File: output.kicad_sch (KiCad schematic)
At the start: 15 parts, among them P12 Conn_01x03_Socket, P13 Conn_01x03_Socket, P14 Conn_01x03_Socket, P27 Conn_01x03_Socket, U4 ULN2003AID

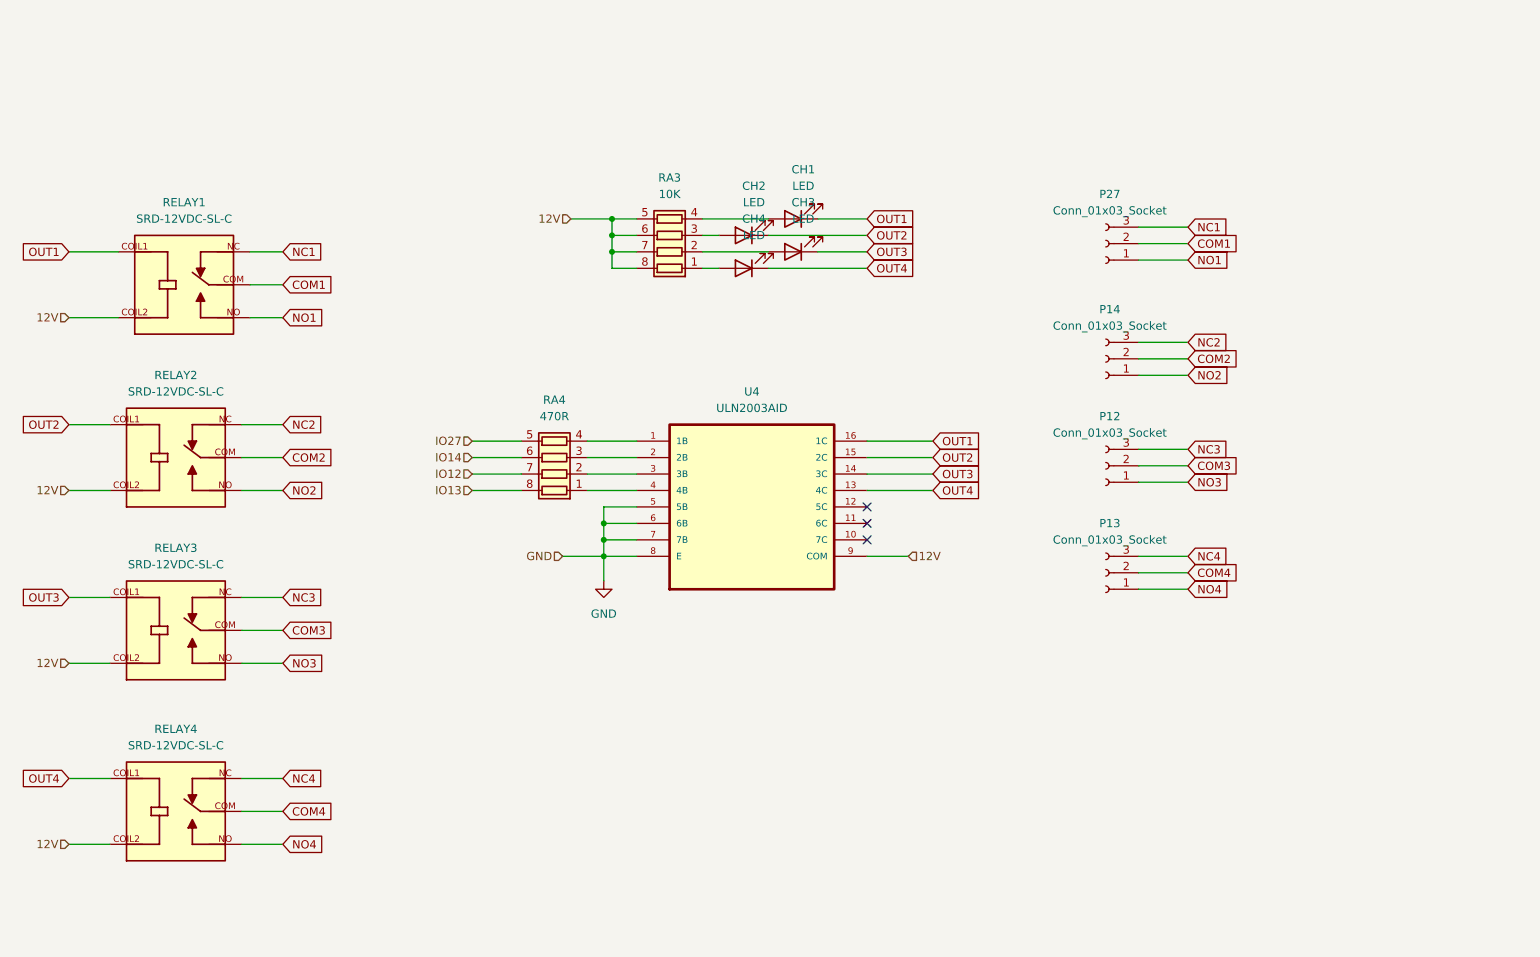
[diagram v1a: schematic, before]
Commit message: relacion de gpios, inicio de esquematico-salidas en proceso
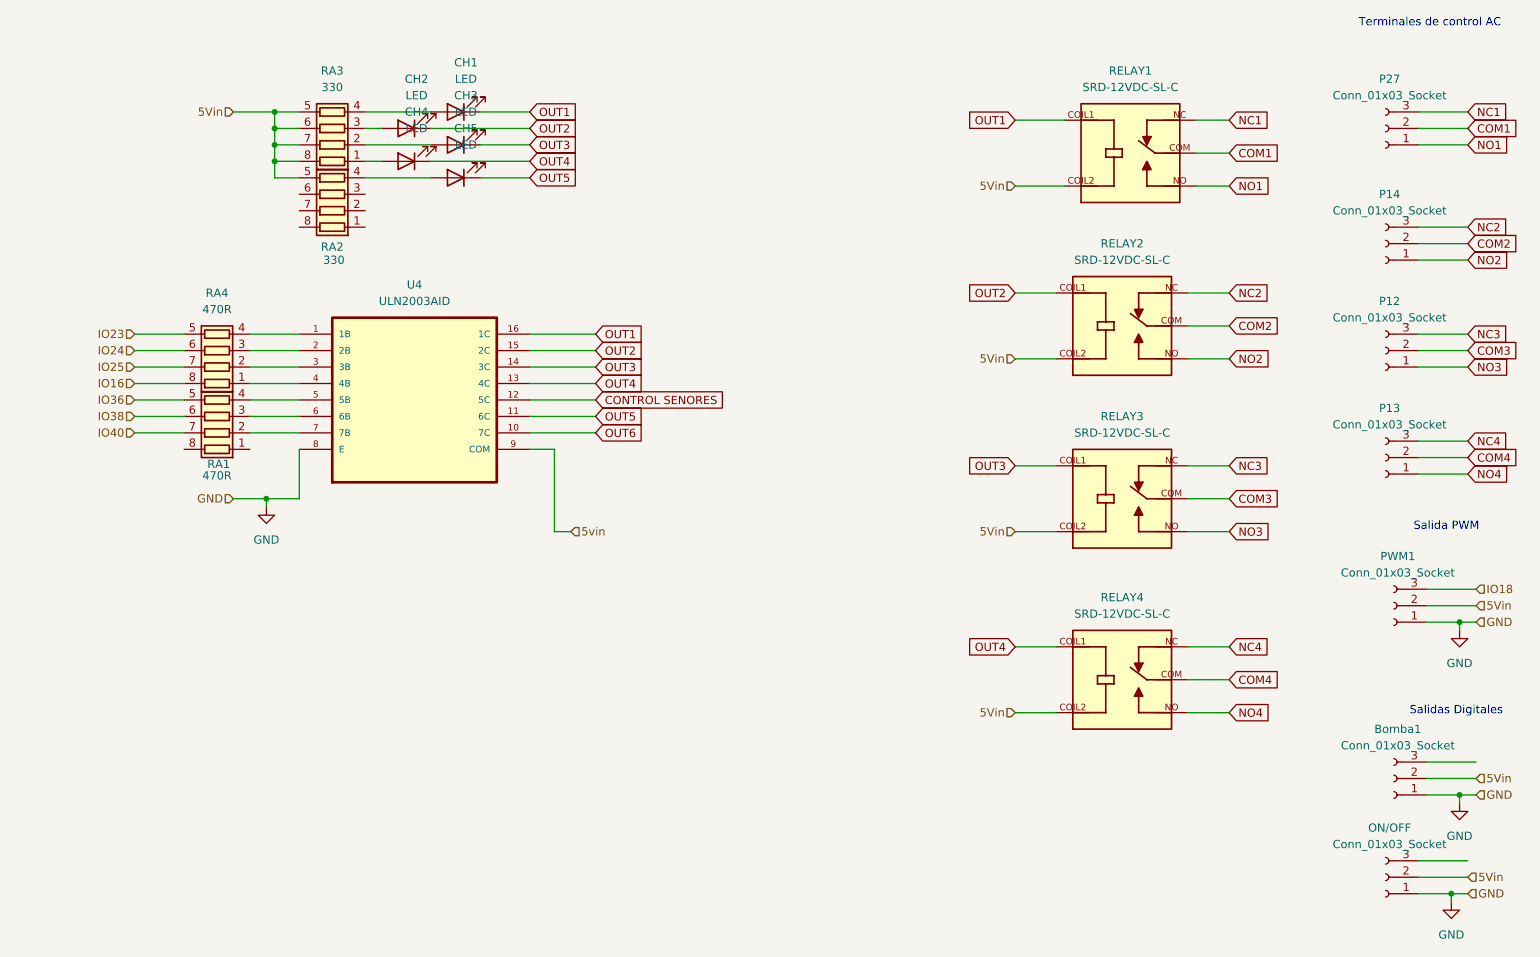
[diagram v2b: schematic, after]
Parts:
- added Bomba1, ON/OFF, PWM1: Conn_01x03_Socket, Connector_PinHeader_2.54mm:PinHeader_1x03_P2.54mm_Vertical, symbol Connector:Conn_01x03_Socket
- added CH5: LED, LED_SMD:LED_1206_3216Metric_Pad1.42x1.75mm_HandSolder, symbol Device:LED
- added RA1: 470R, Resistor_SMD:R_Array_Convex_4x1206, symbol Device:R_Pack04
- added RA2: 330, Resistor_SMD:R_Array_Convex_4x1206, symbol Device:R_Pack04
- RA3: value 10K -> 330
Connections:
- net GND: now also Bomba1.1 (Pin_1), ON/OFF.1 (Pin_1), PWM1.1 (Pin_1); no longer U4.5 (5B), U4.6 (6B), U4.7 (7B)
- net OUT6: now reaches U4.10 (7C)
- net OUT5: now reaches U4.11 (6C)
- net OUT5: now also CH5.1 (K)
- net CONTROL SENORES: now reaches U4.12 (5C)
- net 12V renamed 5Vin
- net 5Vin: now also Bomba1.2 (Pin_2), ON/OFF.2 (Pin_2), PWM1.2 (Pin_2), RA2.5 (R4.2); no longer U4.9 (COM)
- net IO12 renamed IO25
- net IO13 renamed IO16
- net IO14 renamed IO24
- net IO27 renamed IO23
- new net: CH5.2 (A), RA2.4 (R4.1)
- new net: RA1.2 (R2.1), U4.7 (7B)
- new net: RA1.3 (R3.1), U4.6 (6B)
- new net: RA1.4 (R4.1), U4.5 (5B)
- new net 5vin: U4.9 (COM)
- new net IO18: PWM1.3 (Pin_3)
- new net IO36: RA1.5 (R4.2)
- new net IO38: RA1.6 (R3.2)
- new net IO40: RA1.7 (R2.2)
- no-connect marks 3 -> 0
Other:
- note added: "Salida PWM"
- note added: "Salidas Digitales"
- note added: "Terminales de control AC"
- moved on the sheet: CH1, CH2, CH3, CH4, P12, P13, P14, P27, RA3, RA4, RELAY1, RELAY2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

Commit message: 0
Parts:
- U4: footprint ULN2003AID:SOIC127P600X175-16N -> (none)
- renumbered ON/OFF to ON/OFF1
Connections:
- net IO38: now also Bomba1.3 (Pin_3); no longer RA1.6 (R3.2)
- net IO40: now also ON/OFF1.3 (Pin_3); no longer RA1.7 (R2.2)
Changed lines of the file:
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@@
+		)
+	)
+	(hierarchical_label "IO40"
+		(shape input)
+		(at 252.73 151.13 0)
+		(effects
+			(font
+				(size 1.27 1.27)
+			)
+			(justify left)
 		)
 	)
@@
 		)
 	)
-	(hierarchical_label "IO40"
-		(shape input)
-		(at 46.99 85.09 180)
-		(effects
-			(font
-				(size 1.27 1.27)
-			)
-			(justify right)
-		)
-	)
 	(hierarchical_label "5Vin"
 		(shape input)
@@
 		)
 	)
+	(hierarchical_label "IO38"
+		(shape input)
+		(at 254 135.89 0)
+		(effects
+			(font
+				(size 1.27 1.27)
+			)
+			(justify left)
+		)
+	)
 	(hierarchical_label "IO25"
 		(shape input)
@@
 		(shape input)
 		(at 46.99 77.47 180)
-		(effects
-			(font
-				(size 1.27 1.27)
-			)
-			(justify right)
-		)
-	)
-	(hierarchical_label "IO38"
-		(shape input)
-		(at 46.99 82.55 180)
 		(effects
 			(font
@@
 		(dnp no)
 		(fields_autoplaced yes)
-		(property "Reference" "ON/OFF"
+		(property "Reference" "ON/OFF1"
 			(at 240.665 146.05 0)
 			(effects
@@
 			(project "electronica"
 				(path "/a1c80da3-9403-4ec6-a34a-1db23a22b009/b24daec0-e332-4966-b9aa-de928157d88c"
-					(reference "ON/OFF")
+					(reference "ON/OFF1")
 					(unit 1)
 				)
@@
 			)
 		)
-		(property "Footprint" "ULN2003AID:SOIC127P600X175-16N"
+		(property "Footprint" ""
 			(at 90.17 80.01 0)
-			(effects
-				(font
-					(size 1.27 1.27)
-				)
-				(justify bottom)
-				(hide yes)
-			)
-		)
-		(property "Datasheet" ""
+			(show_name yes)
+			(effects
+				(font
+					(size 1.27 1.27)
+				)
+				(justify bottom)
+			)
+		)
+		(property "Datasheet" "kicad-embed://ULN2003AD.lib"
 			(at 90.17 80.01 0)
 			(effects

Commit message: en proceso de hacer el diseño, coloque el modulo de adc a i2c por que es mas barato que comprar las piezas
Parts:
- U4: footprint (none) -> Package_SO:SOIC-16W_5.3x10.2mm_P1.27mm
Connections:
- net IO36 is gone; now on net IO23: RA1.5 (R4.2)
- net IO18: now also RA4.5 (R4.2)
- net IO23: no longer RA4.5 (R4.2)
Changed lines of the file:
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@@
 		)
 	)
-	(hierarchical_label "IO36"
+	(hierarchical_label "IO23"
 		(shape input)
 		(at 46.99 80.01 180)
@@
 		)
 	)
-	(hierarchical_label "IO23"
+	(hierarchical_label "IO18"
 		(shape input)
 		(at 46.99 69.85 180)
@@
 		(on_board yes)
 		(dnp no)
-		(fields_autoplaced yes)
 		(property "Reference" "U4"
 			(at 90.17 62.23 0)
@@
 			)
 		)
-		(property "Footprint" ""
-			(at 90.17 80.01 0)
+		(property "Footprint" "Package_SO:SOIC-16W_5.3x10.2mm_P1.27mm"
+			(at 94.234 95.504 0)
 			(show_name yes)
 			(effects
